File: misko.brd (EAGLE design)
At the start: 100 x 80 mm, 0 parts

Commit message: - ongoing conversion of splan schematic into eagle
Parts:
- added C1: (no value), resistor:C1206
- added C2, C4, C5, C7, C8, C9: 0.47µF, resistor:C0805
- added C3: 0.1µF, resistor:C1206
- added C6: 0.1µF, resistor:C0805
- added IC1: MC1525TT, microchip:SOT23
- added IC2: FT230XS, ftdichip:SSOP16
- added LED1: (no value), led:SML1206
- added LED2, LED3: yellow, led:SML1206
- added R1: (no value), resistor:R1206
- added R10, R12, R16, R17, R18, R8: 47k, rcl:R0805
- added R11, R13, R19, R20, R21, R9: 1k, rcl:R0805
- added R14, R15: 21, rcl:R0805
- added R2, R3: 3k3, rcl:R0805
- added R4, R5: 1k, resistor:R1206
- added R6, R7: 21, resistor:R1206
- added S1: up, switch-omron:B3F-10XX
- added S2: GPRS push, switch-omron:B3F-10XX
- added S3: right, switch-omron:B3F-10XX
- added S4: left, switch-omron:B3F-10XX
- added S5: Bluetooth, switch-omron:B3F-10XX
- added S6: down, switch-omron:B3F-10XX
- added U1: ATMEGA1281-16AU, Atmel_By_element14_Batch_1-00:QFP80P1600X1600X120-64N
- added U2: SN74HCT14DR, Texas Instruments_By_element14_Batch_1:SOIC127P600X175-14N
- added U3: SN74LVC1G3157DBVR - BT switch, Texas Instruments_By_element14_Batch_1:SOT95P280X145-6N
- added U4: SN74LVC1G3157DBVR - GPS switch, Texas Instruments_By_element14_Batch_1:SOT95P280X145-6N
- added U5: TMP36GRTZ-REEL7, TMP36GRTZ:SOT95P280X145-5N
- added U6: TPS63030DSKT, Texas Instruments_By_element14_Batch_1:SON50P260X260X80-11N
- added U7: MCP73871-2AAI/ML, Microchip-MCP73871-2AAI_ML:QFN50P400X400X100-21N
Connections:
- new net 5V0: IC2.12
- new net ADXL345_INT1_INTERRUPT_PIN: U1.9
- new net ANALOG_SW_CTRL_PIN: U1.18, U3.6, U4.6
- new net AVCC: U1.64
- new net BAT_A_PIN: U1.58
- new net BLUETOOTH_TX: U4.3
- new net BLUETOOTH_WAKEUP_PIN: U1.17
- new net GND: C2.1, C3.2, C4.1, C5.1, C7.1, C8.1, C9.1, IC2.13, IC2.5, R16.1, R17.1, R18.1, R19.1, R21.1, S1.3, S1.4, S2.3, S2.4, S3.3, S3.4, S4.1, S4.2, S4.3, S4.4, S5.1, S5.2, S5.3, S5.4, S6.1, S6.2, S6.3, S6.4, U1.22, U1.53, U1.63, U2.7, U3.2
- new net GPS_GREEN_LED_PIN: U1.42
- new net GPS_POWER_CTL_PIN: U1.32
- new net GPS_RED_LED_PIN: U1.41
- new net GPS_SW_SERIAL_RX: U1.14, U3.1, U4.4
- new net GPS_SW_SERIAL_TX: U1.15, U3.3
- new net GPS_TX: U4.1
- new net GPS_WAKEUP_PIN: U1.19
- new net I2C_SCL_PIN: U1.25
- new net I2C_SDA_PIN: U1.26
- new net JTAG_TCL_PIN: U1.57
- new net JTAG_TDI_PIN: U1.54
- new net JTAG_TDO_PIN: U1.55
- new net JTAG_TMS_PIN: U1.56
- new net MCP73871_CHARGE_STATUS_1_PIN: U1.49
- new net MCP73871_CHARGE_STATUS_2_PIN: U1.50
- new net MCP73871_POWER_GOOD_PIN: U1.51
- new net MENU_BLUETOOTH_POWER_TOGGLE_PIN: U1.36, U2.10
- new net MENU_DOWN_BUTTON_PIN: U1.37, U2.12
- new net MENU_GPRS_PUSH_BUTTON_PIN: U1.39, U2.4
- new net MENU_LEFT_BUTTON_PIN: U1.35, U2.8
- new net MENU_RIGHT_BUTTON_PIN: U1.40, U2.6
- new net MENU_UP_BUTTON_PIN: U1.38, U2.2
- new net N$1: IC1.3
- new net N$10: C3.1, IC2.10, IC2.11, IC2.3
- new net N$12: U5.5
- new net N$14: R8.1, R9.1, S1.1, S1.2
- new net N$16: R12.1, R13.1, S3.1, S3.2
- new net N$2: U4.2
- new net N$21: R10.1, R11.1, S2.1, S2.2
- new net N$3: IC2.1, R2.2
- new net N$4: IC2.7, LED3.C
- new net N$5: IC2.14, LED2.C
- new net N$6: LED3.A, R4.2
- new net N$7: IC2.8, R7.2
- new net N$8: LED2.A, R5.1
- new net N$9: IC2.9, R6.1
- new net PDI_UART0_CTS_PIN: IC2.6, U1.1
- new net PDI_UART0_RX_PIN: R2.1, U1.2
- new net PDI_UART0_TX_PIN: IC2.4, R3.1, R3.2, U1.3
- new net S1: C2.2, R8.2, U2.1
- new net S2: C4.2, R10.2, U2.3
- new net S3: C5.2, R12.2, U2.5
- new net S4: C7.2, R18.2, U2.9
- new net S5: C8.2, R17.2, U2.11
- new net S6: C9.2, R16.2, U2.13
- new net SD_CARD_DETECT_PIN: U1.16
- new net SIM800C_CTS_PIN: U1.29
- new net SIM800C_POWER_PIN: U1.31
- new net SIM800C_RX_PIN: U1.27
- new net SIM800C_STATUS_PIN: U1.30
- new net SIM800C_TX_PIN: U1.28
- new net SPI_FRAM_SS_PIN: U1.10
- new net SPI_MISO_PIN: U1.13
- new net SPI_MOSI_PIN: U1.12
- new net SPI_OLED_A0_PIN: U1.6
- new net SPI_OLED_RESET_PIN: U1.5
- new net SPI_SCK_PIN: U1.11
- new net SPI_SS_ADXL345_PIN: U1.4
- new net SPI_SS_OLED_PIN: U1.7
- new net SPI_SS_SD_CARD_PIN: U1.8
- new net TMP36_SHUTDOWN_PIN: U1.48, U5.4
- new net TMP36_VSENSE_PIN: U1.61, U5.1
- new net USB_D+: R7.1
- new net USB_D-: R6.2
- new net VCC: IC1.1, R11.2, R13.2, R19.2, R20.2, R21.2, R9.2, U1.21, U1.52, U2.14, U3.5, U4.5, U5.2
- new net VCC_SENSE_PIN: U1.60
- new net VSS: U7.10
- new net VSS_2: U7.11
- new net V_USB: R4.1, R5.2
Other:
- board size 100 x 80 mm -> 223.2 x 40.6 mm

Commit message: - further work on eagle schematic
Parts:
- added C10: 0.47µF, resistor:C0805
- added C11, C13: 10µF, resistor:C0805
- added G1: CR2450V, battery:CR2450V
- added NTC: 10k, rcl:R0805
- added R22, R23, R24, R25, R28, R31, R33, R34, R35: 1k, rcl:R0805
- added R26, R29, R30: 47k, rcl:R0805
- added R27: 270k, rcl:R0805
- added R32: 100k, rcl:R0805
- added S7: up, switch-omron:B3F-10XX
- moved C7 76.0 mm to (53.3, -43.2)
- moved C8 76.0 mm to (53.3, -49.5)
- moved C9 76.0 mm to (53.3, -55.9)
- moved R17 76.0 mm to (53.3, -11.4)
- moved R18 76.0 mm to (53.3, -17.8)
- moved R19 76.0 mm to (53.3, -24.1)
- moved R20 76.0 mm to (53.3, -30.5)
- moved R21 76.0 mm to (53.3, -36.8)
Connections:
- removed net N$1: IC1.3
- removed net N$12: U5.5
- removed net VSS: U7.10
- removed net VSS_2: U7.11
- new net AREF: IC1.2, U1.62
- new net N$11: R23.2, R24.1, U7.2
- new net N$13: C13.1, G1.+, R34.1, U7.14, U7.15, U7.16
- new net N$18: R28.1, U7.5
- new net N$19: R27.1, R28.2
- new net N$20: NTC.1, R27.2
- new net N$22: R31.1, U7.13
- new net N$23: R32.1, U7.12
- new net RESET: U1.20
- new net XTAL1: U1.24
- new net XTAL2: U1.23
- net BAT_A_PIN: now also R33.1, R34.2, U1.59; no longer U1.58
- net GND: now also C11.2, C13.2, G1.-, IC1.3, NTC.2, R24.2, R31.2, R32.2, R33.2, R35.2, U5.5, U7.10, U7.11
- net MCP73871_CHARGE_STATUS_1_PIN: now also R30.2, U7.8
- net MCP73871_CHARGE_STATUS_2_PIN: now also R29.2, U7.7
- net MCP73871_POWER_GOOD_PIN: now also R26.2, U7.6
- net VCC: now also C11.1, R23.1, R25.1, R26.1, R29.1, R30.1, U7.1, U7.17, U7.18, U7.19, U7.20, U7.3, U7.4, U7.9
- net VCC_SENSE_PIN: now also R25.2, R35.1

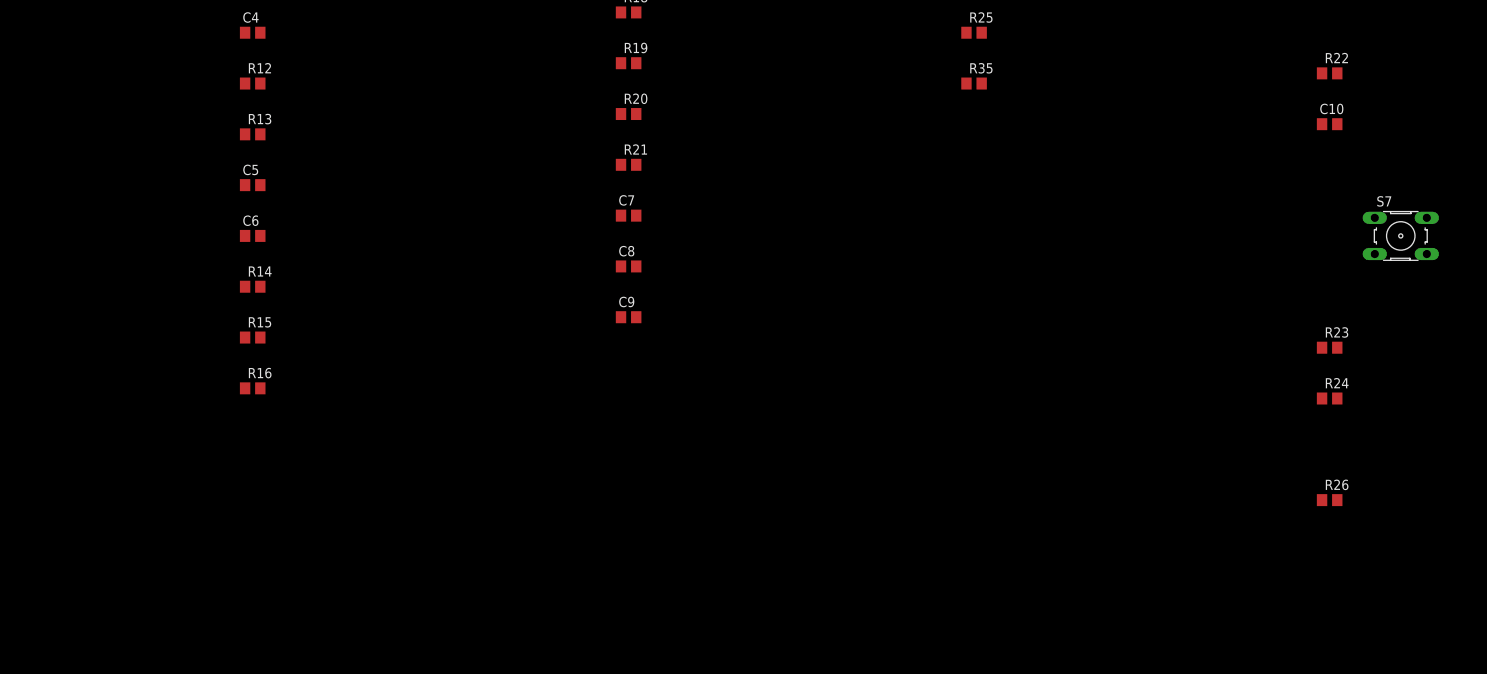
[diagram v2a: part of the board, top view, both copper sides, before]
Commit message: - further porting of schematic to eagle
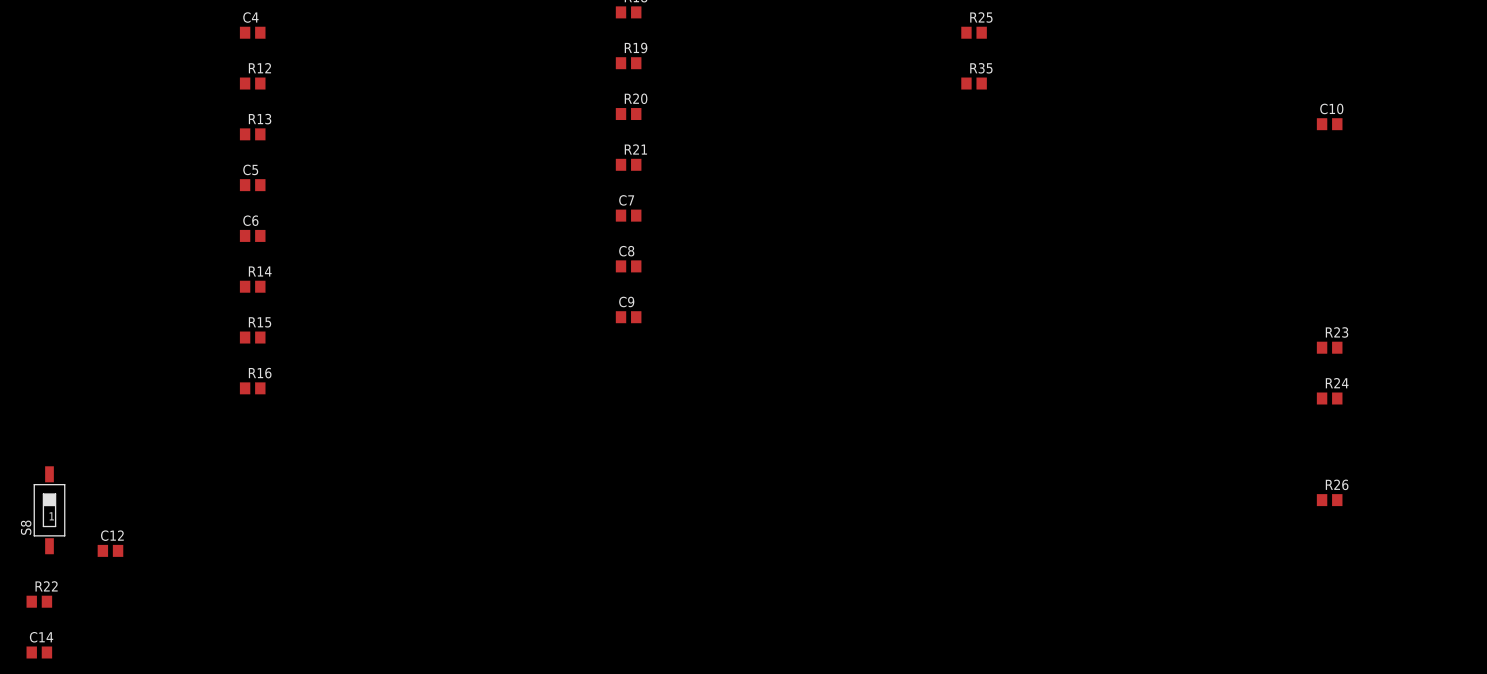
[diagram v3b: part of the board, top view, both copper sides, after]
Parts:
- removed S7: up, switch-omron:B3F-10XX
- added C12: 4.7µF, resistor:C0805
- added C14: 0.1µF, resistor:C0805
- added S8: SWS001, smd-special:SMS-001
- C10: value 0.47µF -> 10µF
- R22, R33, R34: value 1k -> 150k
- R23: value 1k -> 100k
- R24: value 1k -> 270k
- R25, R35: value 1k -> 200k
- moved R22 174.3 mm to (-20.3, -91.4)
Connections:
- new net N$1: R22.1, S8.1, U6.6
- new net N$12: U7.19
- new net N$15: U7.3
- new net N$24: U7.4
- new net N$25: U7.9
- new net N$26: U7.17
- new net N$28: R17.1, R20.1, S5.1, S5.2
- new net N$29: R16.1, R19.1, S6.1, S6.2
- new net N$30: R18.1, R21.1, S4.1, S4.2
- new net VBAT: C11.1, C12.2, S8.2, U6.5, U6.7, U6.8, U7.1, U7.20
- net 5V0: now also R23.1, U7.18
- net GND: now also C10.1, C12.1, C14.2, R22.2, U6.3, U6.9; no longer R16.1, R17.1, R18.1, R19.1, R21.1, S4.1, S4.2, S5.1, S5.2, S6.1, S6.2
- net VCC: now also C10.2, C14.1, U6.1, U6.10; no longer C11.1, R23.1, U7.1, U7.17, U7.18, U7.19, U7.20, U7.3, U7.4, U7.9

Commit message: - further work on eagle schematic
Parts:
- removed C1: (no value), resistor:C1206
- removed G1: CR2450V, battery:CR2450V
- removed R1: (no value), resistor:R1206
- added CN1: (no value), SIM800C:JST-PH-2-SMT
- added G2: CR2450V, battery:CR2450V
- moved S8 182.4 mm to (142.2, 5.08)
- moved R22 179.5 mm to (141.0, -12.7), flipped to the bottom
- moved C12 158.5 mm to (129.5, -12.7), flipped to the bottom
- moved C14 83.8 mm to (63.5, -96.5)
- moved R26 63.1 mm to (181.6, -30.5), flipped to the bottom
- moved R23 59.9 mm to (189.2, -24.1), flipped to the bottom
- moved R24 57.6 mm to (179.1, -22.9), flipped to the bottom
- moved R25 57.2 mm to (153.7, -22.9), flipped to the bottom
- moved R35 56.2 mm to (152.4, -33.0), flipped to the bottom
- moved U6 34.7 mm to (156.2, -5.08), flipped to the bottom
- moved C10 23.3 mm to (162.6, -22.9), flipped to the bottom
- moved R29 15.5 mm to (193.0, -33.0), flipped to the bottom
- moved U1 15.2 mm to (200.7, 20.3)
- moved R30 12.0 mm to (196.8, -45.7), flipped to the bottom
- moved R28 11.7 mm to (234.9, -15.2), flipped to the bottom
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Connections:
- removed net N$13: C13.1, G1.+, R34.1, U7.14, U7.15, U7.16
- removed net N$24: U7.4
- removed net N$25: U7.9
- removed net N$26: U7.17
- new net VBAT+: C13.1, CN1.2, G2.+, R34.1, U7.14, U7.15, U7.16
- net GND: now also CN1.1, G2.-; no longer G1.-
- net N$15: now also U7.17, U7.4, U7.9

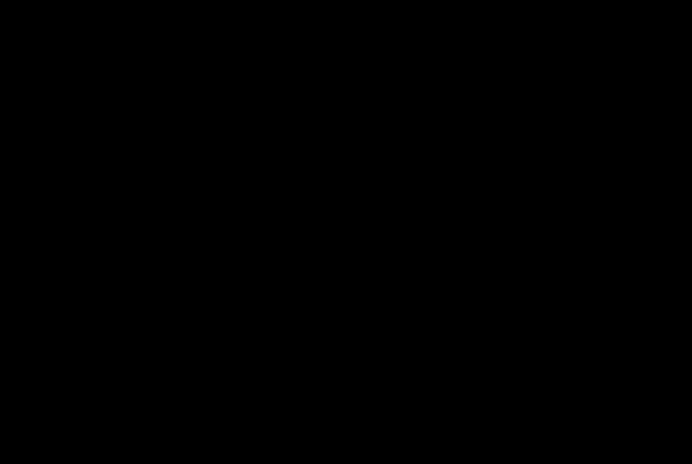
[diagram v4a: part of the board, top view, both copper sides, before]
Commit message: - added ADXL345 Accelerometer.lbr, WIP
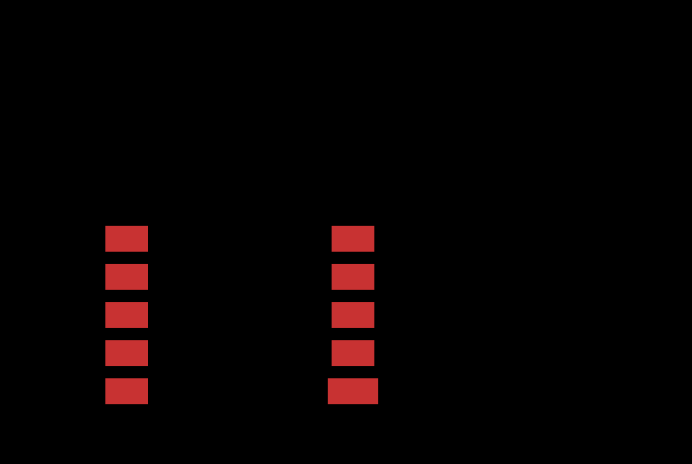
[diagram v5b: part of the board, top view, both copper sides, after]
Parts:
- added U$1: ORG1510-MK4, ORG1510-MK4 GPS module:PACKAGE
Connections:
- net VCC: now also U$1.VCC
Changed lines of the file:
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@@
 <element name="CN1" library="SIM800C" package="JST-PH-2-SMT" value="" x="236.22" y="19.05" rot="MR0"/>
 <element name="G2" library="battery" package="CR2450V" value="CR2450V" x="267.97" y="17.78"/>
+<element name="U$1" library="ORG1510-MK4 GPS module" package="PACKAGE" value="ORG1510-MK4" x="-11.43" y="-100.33"/>
 </elements>
 <signals>
@@
 <contactref element="C14" pad="1"/>
 <contactref element="U1" pad="21"/>
+<contactref element="U$1" pad="VCC"/>
 <wire x1="197.866" y1="12.7" x2="204.2668" y2="27.94" width="0" layer="19" extent="1-1"/>
 <wire x1="184.1246" y1="35.56" x2="204.2668" y2="27.94" width="0" layer="19" extent="1-1"/>
@@
 <wire x1="7.3" y1="-33.02" x2="7.3" y2="-13.97" width="0" layer="19" extent="1-1"/>
 <wire x1="62.55" y1="-96.52" x2="54.29" y2="-36.83" width="0" layer="19" extent="1-1"/>
+<wire x1="-3.8862" y1="-101.6" x2="62.55" y2="-96.52" width="0" layer="19" extent="1-1"/>
 </signal>
 <signal name="GND">

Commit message: - crude positioning of elements on approximate board size
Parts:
- removed G2: CR2450V, battery:CR2450V
- removed LED1: (no value), led:SML1206
- removed LED2, LED3: yellow, led:SML1206
- added ANT2: (no value), discrete:SMD
- added BOTTOM, TOP, X3: FH12-24S-0.5SH, con-hirose:FH12-24S-0.5SH
- added BT_LED: blue, led:SML1206
- added C1: 1µF, resistor:C1206
- added C15: 18pF, resistor:C1206
- added C16: 18pF, rcl:C0805
- added C17, C21, C26, C31, C37, C40: 0.1µF, rcl:C0805
- added C18, C30: 100nF, resistor:C1206
- added C19, C20: 100µF, rcl:C0805
- added C22, C29: 0.1µF, resistor:C0805
- added C23, C24: 15pF, resistor:C0805
- added C25, C27, C28, C38: 10µF, rcl:C0805
- added C32, C33, C34, C35, C36: 4.7µF, rcl:C0805
- added C39: 4.7µF / 25V, rcl:C0805
- added D1: 1N4148, Diode2:D0805
- added D2: (no value), semicon-smd-ipc:SOD80
- added GPRS_LED, GPS_RED_LED: red, led:SML1206
- added GPS_GREEN_LED: green, led:SML1206
- added IC3: LTC4425, LTC4425 Supercap Charger:DFN12
- added IC4: FM25W256-SOIC, FM25W256 FERAM:SOIC08
- added IC5: (no value), 74HCT1G32GW:SOT353/5
- added L1, L5: DJNR6045-100-S, DJNR6045-100S Power Inductor:DJNR6045-100-S
- added L2, L4: 33µH, rcl:L0805
- added L3: 1.5µH, inductor-neosid:MS50
- added OSCI: 8MHz, special:QS
- added Q1: FDN304P, transistor-power:SOT223
- added R1: 220, resistor:R1206
- added R36, R42, R43, R44, R53: 10k, resistor:R1206
- added R37, R38: 100k, resistor:R1206
- added R39, R41, R48, R50, R52: 1k, resistor:R1206
- added R40: 46k, resistor:R1206
- added R45, R46: 270k, rcl:R0805
- added R47: 47k, rcl:R0805
- added R49: 4.7k, rcl:R0805
- added R51: 47k, resistor:R1206
- added R54, R56: 160k, resistor:R1206
- added R55, R57: 910k, resistor:R1206
- added S7: RESET, switch-omron:B3F-10XX
- added SJ1, SJ2: (no value), jumper:SJW
- added SUPERCAP: 1F, capacitor-wima:C5B2.5
- added SV1: (no value), con-lstb:MA05-2
- added SV2: (no value), con-lstb:MA04-1
- added U$2: ORG1510-MK4, ORG1510-MK4 GPS module:PACKAGE
- added U$3: RN-42, EN42-I Bluetooth Module:RN-42
- added U$4: ADXL345, ADXL345 Accelerometer:LGA14
- added U$5: MICROSD_SPI_MODE, Molex SD-47309 SD Card Slot:MICRO_SD_CONNECTOR
- added U$6: V_REG_TPS61040SMD, SparkFun-PowerIC:SOT23-5
- added U$7: 115Q-BCA0, 115Q-BCA0 Micro-SIM Socket:115Q-BCA0
- added USB_RX_LED, USB_TX_LED: yellow, led:SML1206
- added X1: MINI-USB_4P-32005-101, con-cypressindustries:32005-101
- C6: value 0.1µF -> 10µF; device resistor:C0805 -> rcl:C0805
- CN1: value (none) -> LiPo Battery
- NTC: device rcl:R0805 -> rcl:0204/5
- R14: value 21 -> 100k; device rcl:R0805 -> resistor:R1206
- R15: value 21 -> 1k; device rcl:R0805 -> resistor:R1206
- S8: value SWS001 -> POWER_SWITCH
- U$1: value ORG1510-MK4 -> SIM800; device ORG1510-MK4 GPS module:PACKAGE -> SIM800 GPRS Module:SIM800C
- moved NTC 209.5 mm to (60.6, 26.6), turned to 180 degrees
- moved U1 183.0 mm to (17.7, 20.7)
- moved U5 175.2 mm to (10.2, 35.7)
- moved IC1 173.4 mm to (4.45, 36.8)
- moved CN1 167.4 mm to (69.6, 34.6), turned to 90 degrees
- moved R3 165.6 mm to (4.54, 26.4), turned to 90 degrees
- moved U4 163.6 mm to (22.5, 77.8), turned to 180 degrees
- moved R2 162.7 mm to (7.54, 27.5), turned to 90 degrees
- moved U7 158.9 mm to (58.3, 33.2)
- moved U3 153.0 mm to (27.1, 77.7)
- moved R25 150.8 mm to (12.9, 31.3), turned to 180 degrees
- moved R15 150.2 mm to (19.2, 91.2), turned to 90 degrees
- moved R35 148.8 mm to (18.2, 31.3), turned to 180 degrees
- moved C14 145.6 mm to (10.4, 39.1)
- moved R32 138.0 mm to (127.8, 39.7)
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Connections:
- removed net N$2: U4.2
- removed net N$4: IC2.7, LED3.C
- removed net SPI_OLED_A0_PIN: U1.6
- removed net V_USB: R4.1, R5.2
- new net !PFO!: IC3.!PFO!
- new net ANTENNA: ANT2.SIGNAL, C28.2, R52.2
- new net BLUETOOTH_RX: U$3.UART_RX, U3.4
- new net CBUS1: IC2.14, USB_TX_LED.C
- new net CBUS2: IC2.7, USB_RX_LED.C
- new net IREF: R57.2, X3.21
- new net N$100: BOTTOM.23
- new net N$13: R1.2
- new net N$24: IC3.PFI, R37.2, R38.1
- new net N$25: IC3.PROG, R40.2
- new net N$26: IC3.EN, R39.2
- new net N$27: IC3.PFI_RET, R37.1
- new net N$31: C22.2, D1.A, R47.1
- new net N$32: C19.2, C20.2, IC3.VMID
- new net N$33: R42.2, U$3.GPIO7
- new net N$34: BT_LED.A, C6.2, Q1.2, Q1.4, U$3.VDD
- new net N$35: BT_LED.C, R41.2
- new net N$36: R14.1, U$3.GPIO4
- new net N$38: SJ1.2, U$3.GPIO6
- new net N$39: SJ2.2, U$3.RESET
- new net N$40: IC5.Y, U$4.SDA
- new net N$41: GPS_GREEN_LED.C, R46.2
- new net N$43: GPS_RED_LED.C, R45.2
- new net N$44: GPRS_LED.A, R50.2
- new net N$45: R50.1, U$1.NETLIGHT
- new net N$46: C27.2, R52.1, U$1.GSM_ANT
- new net N$47: U$1.GND10, U$1.GND9
- new net N$48: U$1.GND6, U$1.GND7
- new net N$53: L3.2, U6.4
- new net N$54: L3.1, U6.2
- new net N$73: D2.2, L4.1, U$6.1
- new net N$76: C35.1, R55.1, R56.2, U$6.3
- new net N$86: BOTTOM.21
- new net N$87: BOTTOM.22
- new net N$90: TOP.23
- new net N$91: TOP.22
- new net N$92: TOP.21
- new net OLED_POWER_ON-OFF: R54.2, U$6.4
- new net SIM_CLOCK: U$1.SIM_CLK, U$7.CLK
- new net SIM_DATA: C25.1, U$1.SIM_DATA, U$7.I/O
- new net SIM_DETECT: R48.2, U$1.SIM_DET, U$7.CD
- new net SIM_RESET: U$1.SIM_RST, U$7.RST
- new net SIM_VDD: U$1.SIM_VDD, U$7.VPP
- new net SPI_OLED_D/C_PIN: U1.6, X3.10
- new net USB_VBUS: U$1.USB_VBUS
- new net VCOMH: C39.2, X3.22
- new net VGPS: C1.1, IC3.VOUT1, IC3.VOUT2, SUPERCAP.2, U$2.VCC
- new net VOLED: C33.2, C34.2, C35.2, C37.2, C38.2, D2.1, R55.2, X3.23
- new net VUSB: L1.P$2, R4.1, R5.2, X1.1
- net 5V0: now also C18.2, C30.2, L1.P$1, L5.P$2, U7.19
- net ADXL345_INT1_INTERRUPT_PIN: now also U$4.INT1
- net ANALOG_SW_CTRL_PIN: now also BOTTOM.13, TOP.13
- net AVCC: now also C29.2, IC1.1, L2.2
- net BLUETOOTH_TX: now also U$3.UART_TX
- net BLUETOOTH_WAKEUP_PIN: now also Q1.1, R15.1
- net GND: now also BOTTOM.1, BOTTOM.24, C1.2, C15.1, C16.2, C17.2, C18.1, C20.1, C21.1, C22.1, C23.1, C24.1, C25.2, C26.1, C27.1, C28.1, C29.1, C30.1, C31.2, C32.1, C33.1, C34.1, C36.1, C37.1, C38.1, C39.1, C40.1, C6.1, GPRS_LED.C, IC3.GND, IC4.GND, IC5.GND, R14.2, R36.2, R41.1, R42.1, R54.1, R56.1, R57.1, S7.3, S7.4, SJ1.1, SJ2.1, SUPERCAP.1, SV1.10, SV1.2, SV2.1, TOP.1, TOP.24, U$1.GND2, U$1.GND3, U$1.GND4, U$1.GND8, U$2.GND, U$3.GND1, U$3.GND2, U$3.GND3, U$3.GND4, U$3.GPIO3, U$4.GND1, U$4.GND2, U$4.GND3, U$5.GND2, U$5.GND4, U$5.POL, U$5.VSS, U$6.2, U$7.GND1, U$7.GND2, U$7.GND3, U$7.GND4, U$7.GND5, U4.2, X1.4, X3.1, X3.11, X3.12, X3.2, X3.24, X3.3, X3.6, X3.7; no longer G2.-
- net GPS_GREEN_LED_PIN: now also BOTTOM.10, BOTTOM.12, R46.1, TOP.10, TOP.12
- net GPS_POWER_CTL_PIN: now also BOTTOM.18, R1.1, R36.1, TOP.18, U$2.ON_OFF
- net GPS_RED_LED_PIN: now also BOTTOM.11, BOTTOM.9, R45.1, TOP.11, TOP.9
- net GPS_SW_SERIAL_RX: now also BOTTOM.19, TOP.19
- net GPS_SW_SERIAL_TX: now also BOTTOM.20, C15.2, TOP.20, U$2.RX
- net GPS_TX: now also C16.1, U$2.TX
- net GPS_WAKEUP_PIN: now also BOTTOM.17, TOP.17, U$2.WAKEUP
- net I2C_SCL_PIN: now also SV2.3
- net I2C_SDA_PIN: now also SV2.2
- net JTAG_TCL_PIN: now also SV1.1
- net JTAG_TDI_PIN: now also SV1.9
- net JTAG_TDO_PIN: now also SV1.3
- net JTAG_TMS_PIN: now also SV1.5
- net MENU_BLUETOOTH_POWER_TOGGLE_PIN: now also BOTTOM.4, TOP.4
- net MENU_DOWN_BUTTON_PIN: now also BOTTOM.5, TOP.5
- net MENU_GPRS_PUSH_BUTTON_PIN: now also BOTTOM.7, TOP.7
- net MENU_LEFT_BUTTON_PIN: now also BOTTOM.3, TOP.3
- net MENU_RIGHT_BUTTON_PIN: now also BOTTOM.8, TOP.8
- net MENU_UP_BUTTON_PIN: now also BOTTOM.6, TOP.6
- net N$12: now also IC2.4, R3.2; no longer U7.19
- net N$5: now also L5.P$1, SV2.4; no longer IC2.14, LED2.C
- net N$6: now also USB_RX_LED.A; no longer LED3.A
- net N$8: now also USB_TX_LED.A; no longer LED2.A
- net PDI_UART0_CTS_PIN: now also BOTTOM.16, TOP.16
- net PDI_UART0_RX_PIN: now also BOTTOM.14, TOP.14
- net PDI_UART0_TX_PIN: now also BOTTOM.15, TOP.15; no longer IC2.4, R3.2
- net RESET: now also R47.2, R49.2, S7.1, S7.2, SV1.6
- net SD_CARD_DETECT_PIN: now also U$5.DET
- net SIM800C_CTS_PIN: now also U$1.UART1_CTS
- net SIM800C_POWER_PIN: now also R48.1, R51.1, U$1.PWRKEY, U$1.VDD_EXT
- net SIM800C_RX_PIN: now also U$1.UART1_TXD
- net SIM800C_STATUS_PIN: now also U$1.STATUS
- net SIM800C_TX_PIN: now also U$1.UART1_RXD
- net SPI_FRAM_SS_PIN: now also IC4.!CS!, R44.1
- net SPI_MISO_PIN: now also IC4.SO, U$4.SDO, U$5.DAT0
- net SPI_MOSI_PIN: now also IC4.SI, IC5.B, U$5.CMD, X3.14
- net SPI_OLED_RESET_PIN: now also X3.9
- net SPI_SCK_PIN: now also IC4.SCK, U$4.SCL, U$5.CLK, X3.13
- net SPI_SS_ADXL345_PIN: now also IC5.A, R43.2, U$4.!CS!
- net SPI_SS_OLED_PIN: now also X3.8
- net SPI_SS_SD_CARD_PIN: now also R53.1, U$5.CD/DAT3
- net USB_D+: now also X1.3
- net USB_D-: now also X1.2
- net VBAT: now also C26.2, R51.2, U$1.VBAT1, U$1.VBAT2, U$1.VRTC
- net VBAT+: no longer G2.+
- net VCC: now also BOTTOM.2, C17.1, C19.1, C21.2, C31.1, C32.2, C36.2, C40.2, D1.C, GPS_GREEN_LED.A, GPS_RED_LED.A, IC3.FB, IC3.SEL, IC3.VCC1, IC3.VCC2, IC4.!HOLD!, IC4.!WP!, IC4.VCC, IC5.VCC, L2.1, L4.2, Q1.3, R15.2, R38.2, R39.1, R40.1, R43.1, R44.2, R49.1, R53.2, SV1.4, TOP.2, U$4.VCC, U$4.VDD, U$5.VDD, U$6.5, U$7.VCC, X3.5; no longer IC1.1, U$1.VCC
- net XTAL1: now also C24.2, OSCI.1
- net XTAL2: now also C23.2, OSCI.2
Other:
- board size 223.2 x 40.6 mm -> 75 x 88 mm
